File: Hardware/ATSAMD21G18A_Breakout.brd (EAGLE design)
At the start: 50.3 x 17.8 mm, 35 parts, among them J2 GRPB052VWVN-RC, J3 MF-CON-2.54mm-01x14, J4 MF-CON-2.54mm-01x14, J5 MF-CON-2.54mm-01x06, J6 MF-CON-2.54mm-01x06, SW1 MF-SW-TACT-4.2MM, U1 ATSAMD21G18A, U2 IP4234CZ6,125, U3 BQ24165RGET, U4 MF-REG-SOT235-3.3V-300mA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

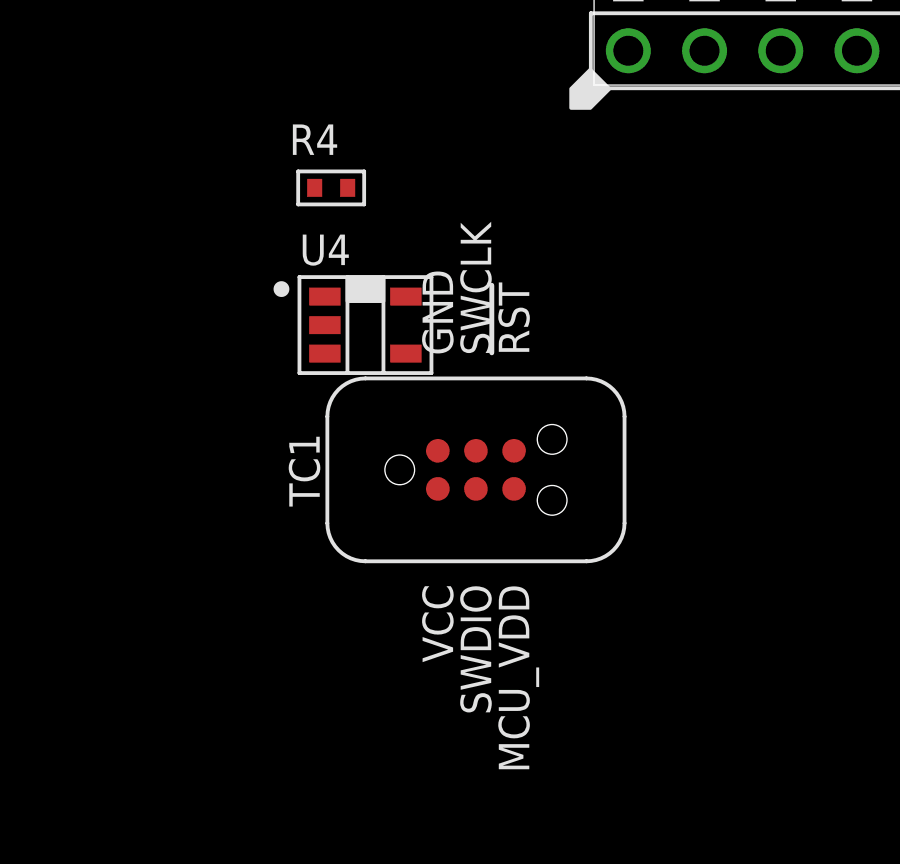
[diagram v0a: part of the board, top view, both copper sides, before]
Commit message: removed tag connect and added LDK320AM33R for the LDO
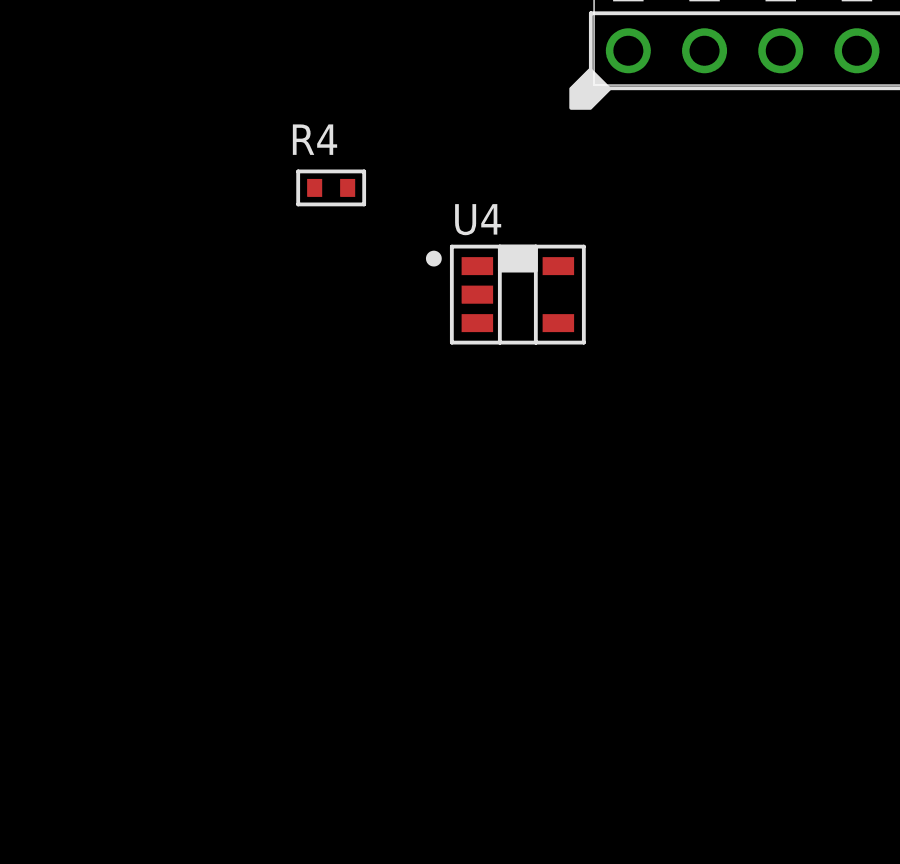
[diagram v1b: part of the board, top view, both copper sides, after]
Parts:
- removed TC1: TC2030-IDC-NL, MF_Connectors:TC2030-IDC-NL
- U4: value MF-REG-SOT235-3.3V-300mA -> LDK320AM33R
- moved U4 5.18 mm to (-2.54, -6.99)
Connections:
- removed net SWO: TC1.P$5
- net !RESET: no longer TC1.P$6
- net 3.3V: no longer TC1.P$1
- net GND: no longer TC1.P$2
- net SWCLK: no longer TC1.P$4
- net SWDIO: no longer TC1.P$3
